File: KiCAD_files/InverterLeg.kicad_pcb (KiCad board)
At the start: 4 copper layers, 29 x 75 mm, 63 parts, among them J803 Conn_01x01_Pin, J806 Conn_01x01_Pin, J811 Screw_Terminal_01x01, J814 Screw_Terminal_01x01, J817 Screw_Terminal_01x01, J825 Conn_02x02_Top_Bottom, J827 Conn_02x02_Top_Bottom, J831 Conn_02x02_Top_Bottom, Q801 IPT60R055CM8, Q802 IPT60R055CM8, T801 CMB1670V, T802 CMB1670V, U603 UCC21222DR, U704 VPS8701B, U707 VPS8701B, U811 TMP117xxDRV, U815 TMP117xxDRV

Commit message: First routing complete.
Signed-off-by: Jean Alinei <jean.alinei@owntech.org>
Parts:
- removed R710: 4.7k, Resistor_SMD:R_0603_1608Metric
- added C718: 10uF, Capacitor_SMD:C_0805_2012Metric, F.Cu at (142.4, 91.2)
- added C719: 10uF, Capacitor_SMD:C_0805_2012Metric, F.Cu at (159.4, 90.7)
- added R610: 51R, Resistor_SMD:R_0402_1005Metric, F.Cu at (159.2, 96.5)
- added R611: 51R, Resistor_SMD:R_0402_1005Metric, F.Cu at (159.3, 97.4)
- added R612: 51R, Resistor_SMD:R_0402_1005Metric, F.Cu at (139.5, 96.1)
- added R613: 51R, Resistor_SMD:R_0402_1005Metric, F.Cu at (139.5, 95.2)
- added U801: LT1761-SD, Package_TO_SOT_SMD:TSOT-23-5, F.Cu at (158.6, 94.4)
- added U802: LT1761-SD, Package_TO_SOT_SMD:TSOT-23-5, F.Cu at (138.4, 93.2)
- U603: footprint Package_SO:SOIC-16W_7.5x10.3mm_P1.27mm -> Footprints:SOIC-16W_7.5x10.3mm_P1.27mm
- moved C734 3.10 mm to (155.8, 94.2), turned to -90 degrees
- moved C614 3.00 mm to (144.9, 89.5)
- moved C616 3.00 mm to (141.8, 89.1), turned to 0 degrees
- moved D710 2.66 mm to (156.4, 96.8)
- moved R605 2.60 mm to (154.7, 73.9)
- moved C602 2.60 mm to (152.3, 77.6)
- moved C604 2.60 mm to (152.3, 76.1)
- moved C605 2.60 mm to (147.0, 76.8)
- moved C607 2.60 mm to (149.3, 76.1)
- moved C703 2.60 mm to (155.4, 76.1)
- moved J831 2.60 mm to (148.6, 72.0)
- moved R606 2.60 mm to (153.1, 73.9)
- moved R609 2.60 mm to (149.3, 77.6)
- moved T801 2.60 mm to (150.0, 94.1)
- moved U603 2.60 mm to (151.2, 84.3)
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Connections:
- C717 pad 1: /12V_{LS} -> /12V_{LSRAW}
- C731 pad 1: /12V_{LS} -> /12V_{LSRAW}
- C734 pad 1: /12V_{HS} -> Net-(D709-K)
- D703 pad 1: /12V_{LS} -> /12V_{LSRAW}
- D704 pad 1: /12V_{LS} -> /12V_{LSRAW}
- D709 pad 1: /12V_{HS} -> Net-(D709-K)
- D710 pad 1: /12V_{HS} -> Net-(D709-K)
- L706 pad 1: /12V_{LS} -> /12V_{LSRAW}
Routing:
- net /GND_{LS}: track 0.00 -> 25.8 mm, vias 6 -> 11
- net /12V_{LS}: track 0.00 -> 16.5 mm, vias 1 -> 4
- net Net-(U704-VIN): track 0.00 -> 8.29 mm
- net /K_{SWN}: track 5.17 -> 13.0 mm, vias 3 -> 5
- net /12V_{PGND}: track 0.00 -> 7.55 mm
- net /12V_{HS}: track 2.80 -> 9.07 mm
- net Net-(U707-VIN): track 6.83 -> 12.3 mm
- net Net-(U704-VD1): track 0.00 -> 3.73 mm
- net Net-(U704-VD2): track 0.00 -> 3.37 mm
- net /5V_{DGND}: track 25.6 -> 22.4 mm
- net Net-(U707-VD1): track 0.00 -> 3.14 mm
- net Net-(U707-VD2): track 0.00 -> 2.86 mm
- net Net-(D709-K): track 0.00 -> 2.75 mm, vias 0 -> 2
- net /EN: track 0.00 -> 2.73 mm
- net /PWM_{LS}: track 20.1 -> 17.5 mm
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- added copper zone on F.Cu, net /12V_{HS}
- added copper zone on F.Cu, net /12V_{LSRAW}
- added copper zone on B.Cu, net /GND_{LS}
- added copper zone on B.Cu, net /SWN
- added copper zone on B.Cu, net /V_{IHigh_PGND}
- added copper zone on F.Cu, net Net-(D709-K)
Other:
- board size 29 x 75 mm -> 29 x 73 mm

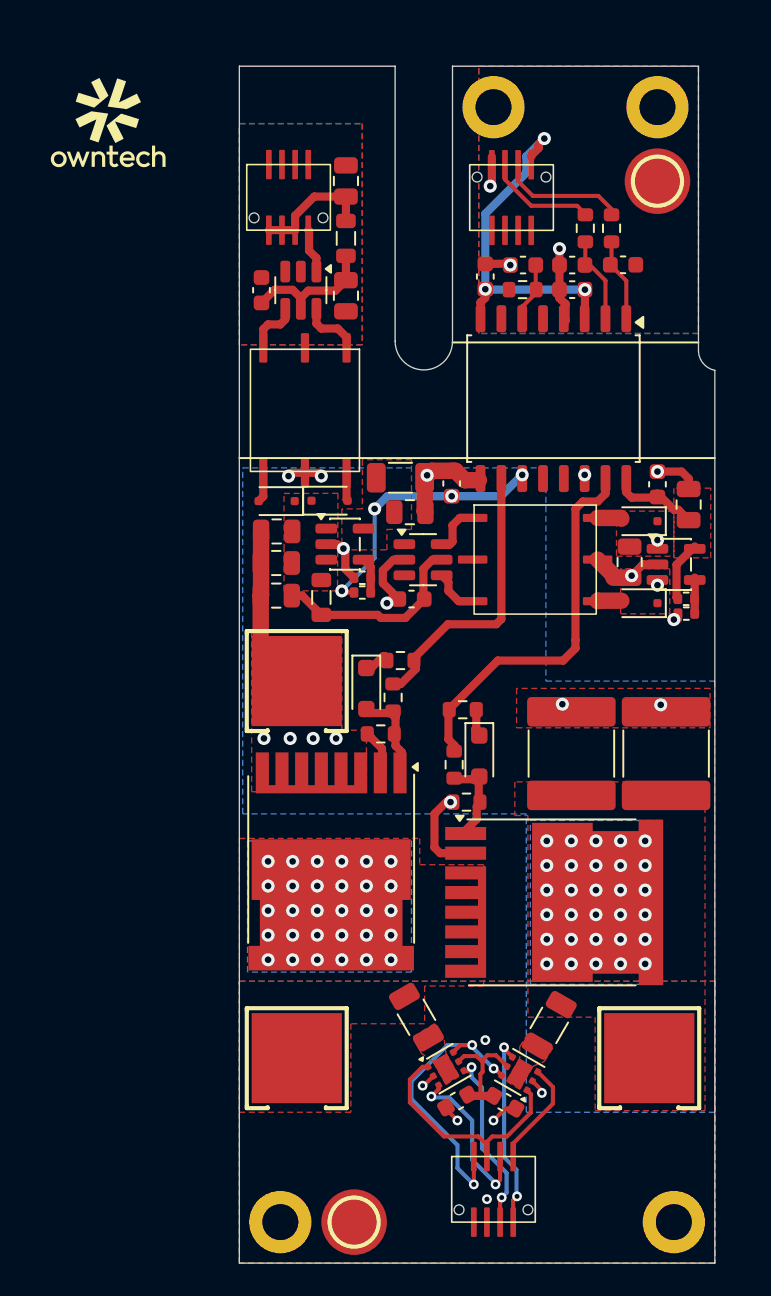
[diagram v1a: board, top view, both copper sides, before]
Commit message: Added gate coax. Added IPC2221 B1 rules. Changed diode footprints. Completed layout.
Signed-off-by: Jean Alinei <jean.alinei@owntech.org>
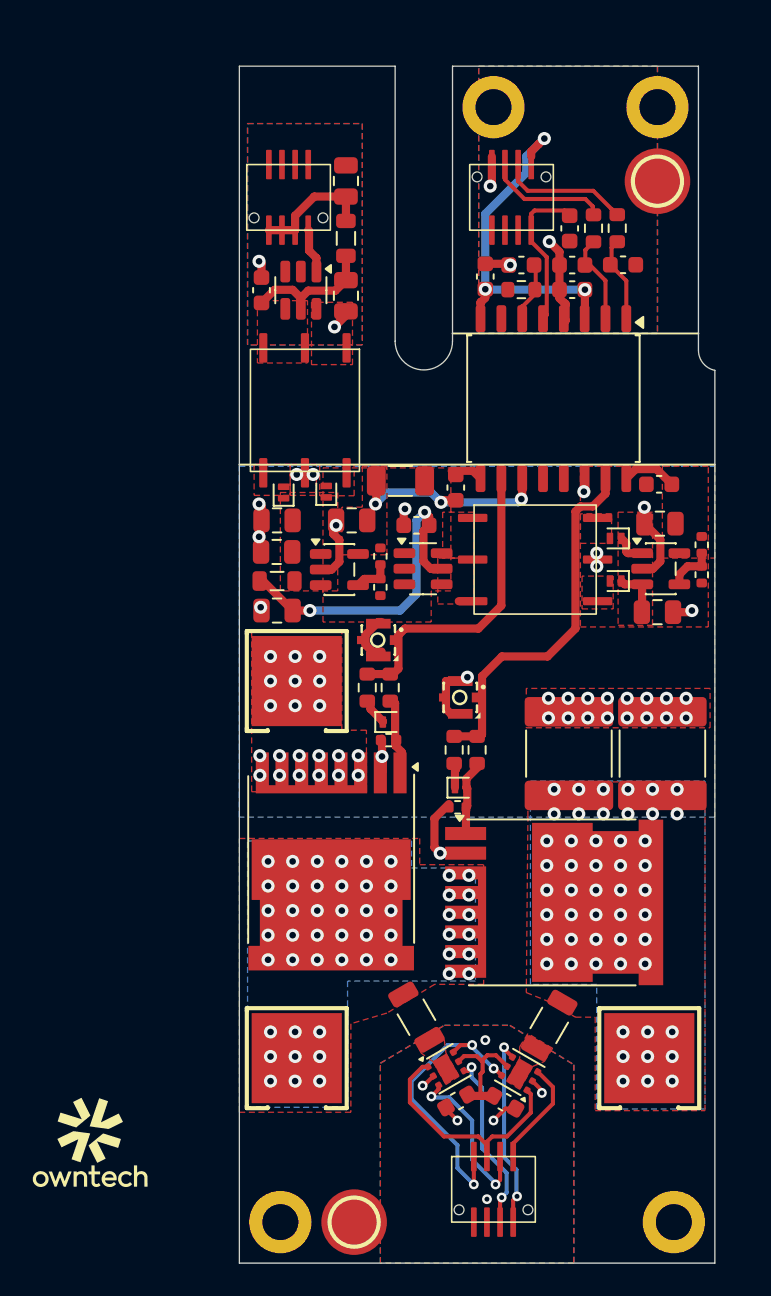
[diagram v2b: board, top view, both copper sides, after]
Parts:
- added C608: 100nF, Capacitor_SMD:C_0603_1608Metric, F.Cu at (152.1, 73.9)
- added J801: Conn_Coaxial_Small, Footprints:IPEX-SMD_4P-L1.7-W1.7-LS2.0-L-4, F.Cu at (145.5, 102.5)
- added J802: Conn_Coaxial_Small, Footprints:IPEX-SMD_4P-L1.7-W1.7-LS2.0-L-4, F.Cu at (140.5, 99.0)
- D601: footprint Diode_SMD:D_SOD-323_HandSoldering -> Diode_SMD:D_SOD-882
- D602: value PMEG3010CEJ,115 -> ~; footprint Diode_SMD:D_SOD-323_HandSoldering -> Diode_SMD:D_SOD-882
- D703, D704, D709, D710: footprint Diode_SMD:D_SOD-323F -> Diode_SMD:D_SOD-882
- R607, R608: footprint Resistor_SMD:R_0603_1608Metric -> Resistor_SMD:R_0402_1005Metric
- TJ801, TJ804: footprint Resistor_SMD:R_1206_3216Metric -> Footprints:THJP_1206_3216Metric
- moved G*** 62.2 mm to (122.9, 128.9)
- moved G*** 62.2 mm to (122.9, 131.7)
- moved C733 4.51 mm to (142.8, 92.0)
- moved C718 3.59 mm to (138.8, 91.7), turned to 180 degrees
- moved C734 3.49 mm to (157.5, 97.3), turned to 0 degrees
- moved R610 3.43 mm to (160.2, 93.2), turned to 90 degrees
- moved L706 2.88 mm to (134.3, 95.4), turned to 180 degrees
- moved R603 2.61 mm to (139.8, 101.9), turned to -90 degrees
- moved R611 2.55 mm to (160.2, 95.0), turned to 90 degrees
- moved R601 2.51 mm to (145.1, 105.7), turned to -90 degrees
- moved R612 2.47 mm to (140.6, 93.9), turned to 90 degrees
- moved D601 2.45 mm to (141.1, 104.0), turned to 0 degrees
- moved D602 2.24 mm to (145.5, 108.0), turned to 0 degrees
- moved C719 2.10 mm to (157.7, 91.9), turned to 180 degrees
- moved D710 1.98 mm to (154.9, 95.4)
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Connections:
- C614 pad 2: /GND_{LS} -> /K_{GNDLS}
- C616 pad 2: /GND_{LS} -> /K_{GNDLS}
- C717 pad 2: /GND_{LS} -> /K_{GNDLS}
- C718 pad 2: /GND_{LS} -> /K_{GNDLS}
- C731 pad 2: /GND_{LS} -> /K_{GNDLS}
- C732 pad 2: /GND_{LS} -> /K_{GNDLS}
- C733 pad 2: /GND_{LS} -> /K_{GNDLS}
- J831 pad 8: unconnected-(J831-Pin_8-Pad8) -> /DIS
- Q801 pad 2: Net-(Q801-DS) -> /K_{GNDLS}
- R608 pad 1: Net-(Q801-DS) -> /K_{GNDLS}
- R613 pad 1: /GND_{LS} -> /K_{GNDLS}
- T802 pad 5: /GND_{LS} -> /K_{GNDLS}
- U603 pad 9: /GND_{LS} -> /K_{GNDLS}
- U707 pad 2: /GND_{LS} -> /K_{GNDLS}
- U802 pad 2: /GND_{LS} -> /K_{GNDLS}
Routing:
- net /GND_{LS}: track 25.8 -> 0.00 mm, vias 11 -> 37
- net /K_{GNDLS}: track 0.00 -> 17.7 mm, vias 0 -> 8
- net /DIS: track 0.00 -> 9.45 mm
- net Net-(U707-VIN): track 12.3 -> 20.5 mm, vias 0 -> 2
- net /12V_{HS}: track 9.07 -> 3.40 mm
- net Net-(U704-VD1): track 3.73 -> 0.00 mm
- net /K_{SWN}: track 13.0 -> 16.5 mm, vias 5 -> 7
- net Net-(U704-VD2): track 3.37 -> 0.00 mm
- net /12V_{LS}: track 16.5 -> 13.2 mm, vias 4 -> 3
- net Net-(U707-VD1): track 3.14 -> 0.00 mm
- net Net-(Q801-DS): track 2.62 -> 0.00 mm
- net /PGND: track 4.60 -> 6.89 mm, vias 6 -> 8
- net Net-(U707-VD2): track 2.86 -> 0.85 mm
- net Net-(D704-A): track 1.84 -> 0.00 mm
- net Net-(D703-A): track 1.72 -> 0.00 mm
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- added copper zone on F.Cu, net /K_{GNDLS}
- added copper zone on In1.Cu, net /K_{GNDLS}
- added copper zone on F.Cu, net /K_{SWN}
- added copper zone on F.Cu, net Net-(D703-A)
- added copper zone on F.Cu, net Net-(D704-A)
- added copper zone on F.Cu, net Net-(D709-A)
- added copper zone on F.Cu, net Net-(D710-A)
- added copper zone on F.Cu, net Net-(U704-VD1)
- added copper zone on F.Cu, net Net-(U704-VD2)
- added copper zone on F.Cu, net Net-(U707-VD1)
- added copper zone on F.Cu, net Net-(U707-VD2)

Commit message: Added SMTSO footprints to replace cube screw terminals. Added header for optional fan
Signed-off-by: Jean Alinei <jean.alinei@owntech.org>
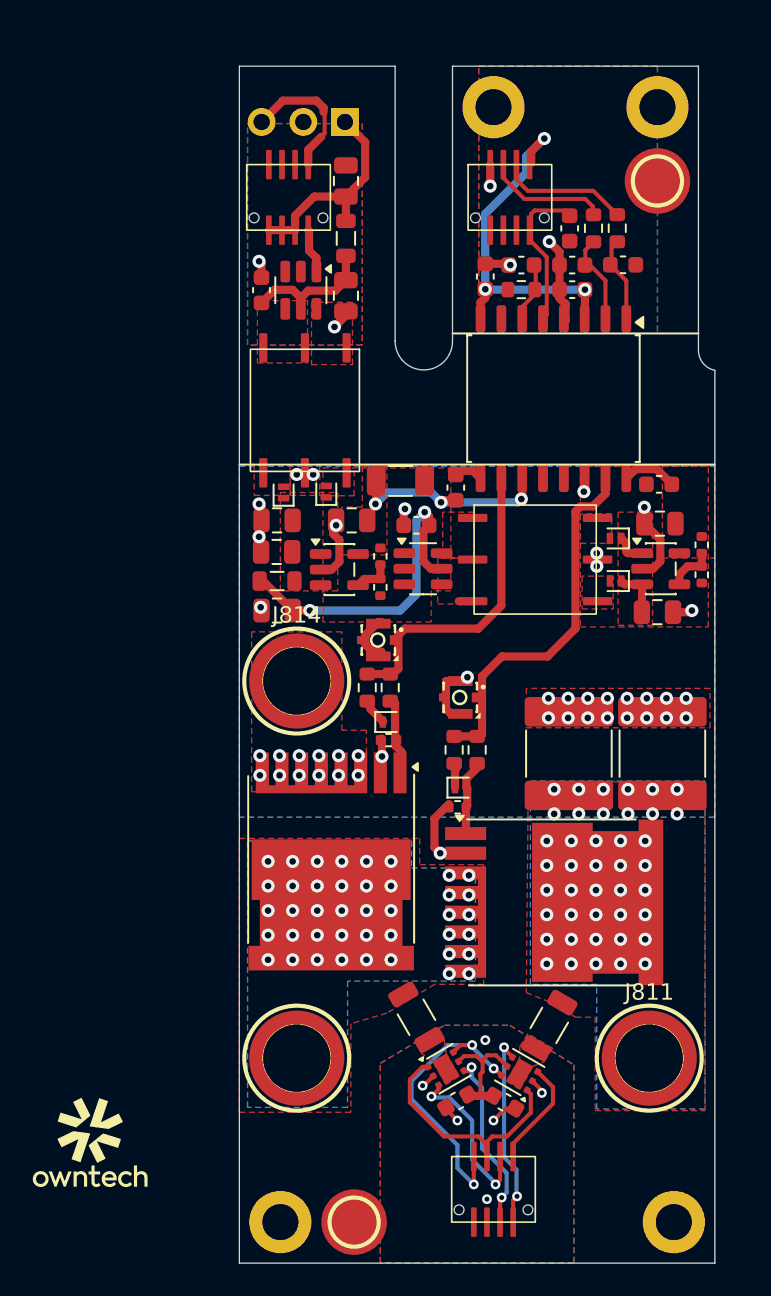
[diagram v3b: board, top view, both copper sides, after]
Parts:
- added J804: Conn_01x03_Socket, Connector_PinHeader_2.54mm:PinHeader_1x03_P2.54mm_Vertical, B.Cu at (138.4, 67.4)
- J811, J814, J817: footprint Footprints:SMD_L5.0-W5.0_CON1_5X5_SMD -> Footprints:SMD-1_BD5.5-D4.0_H5
- moved J831 0.10 mm to (148.5, 72.0), turned to 0 degrees
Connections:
- J825 pad 5: /PGND -> /SPEED
- J831 pad 1: /5V_{DGND} -> unconnected-(J831-Pin_1-Pad1)
- J831 pad 2: /PWMH_{MCU} -> unconnected-(J831-Pin_2-Pad2)
- J831 pad 3: /PWML_{MCU} -> unconnected-(J831-Pin_3-Pad3)
- J831 pad 4: DGND -> /DIS
- J831 pad 5: unconnected-(J831-Pin_5-Pad5) -> /5V_{DGND}
- J831 pad 6: unconnected-(J831-Pin_6-Pad6) -> /PWMH_{MCU}
- J831 pad 7: unconnected-(J831-Pin_7-Pad7) -> /PWML_{MCU}
- J831 pad 8: /DIS -> DGND
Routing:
- net /SPEED: track 0.00 -> 8.40 mm
- net /12V_{PGND}: track 7.55 -> 13.1 mm
- net Net-(U603-DT): track 4.01 -> 3.01 mm
- net DGND: track 8.84 -> 8.31 mm
- net /V_{IHigh_PGND}: vias 51 -> 42
- net /SWN: vias 51 -> 42
- net /GND_{LS}: vias 37 -> 28

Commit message: Tidied up schematic - Final height for SMTSO 5mm
Signed-off-by: Jean Alinei <jean.alinei@owntech.org>
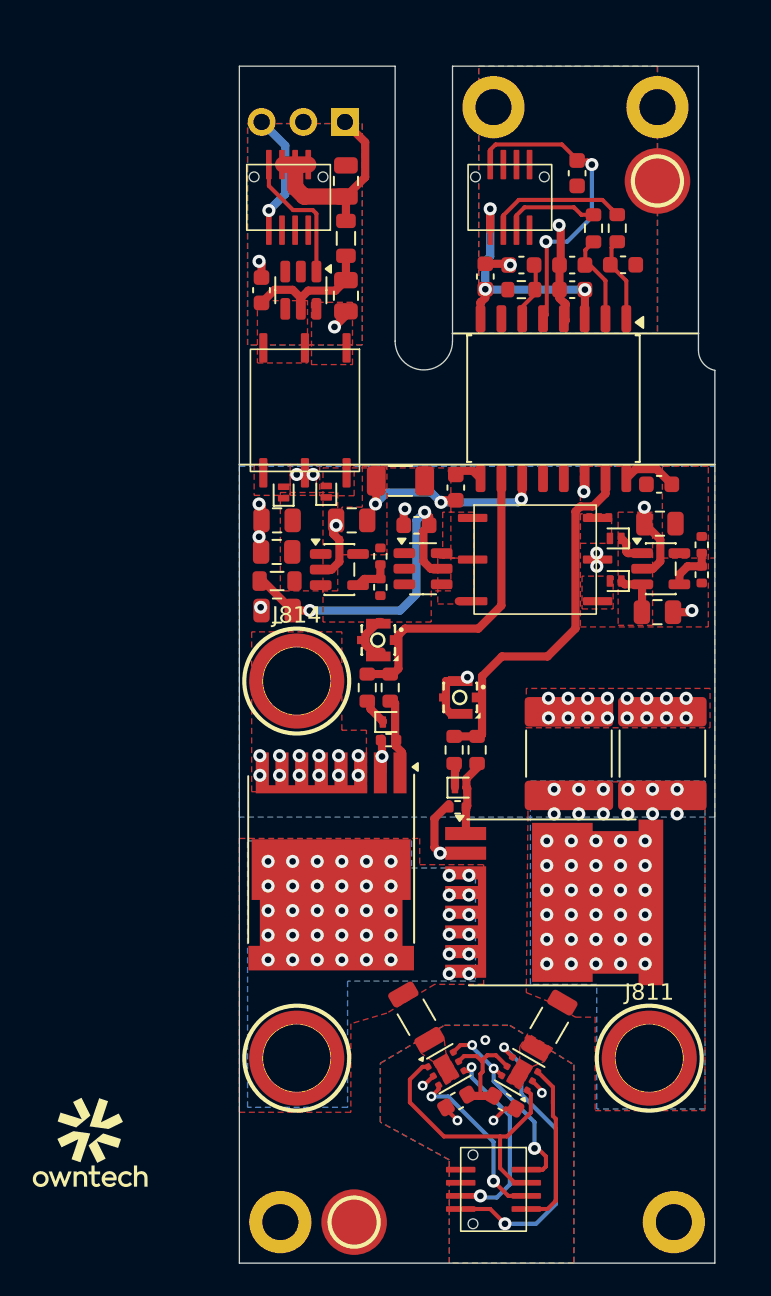
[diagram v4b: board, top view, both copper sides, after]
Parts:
- moved C608 3.40 mm to (152.6, 70.5)
- turned J825 to 180 degrees
- turned J827 to -90 degrees
- turned J831 to 180 degrees
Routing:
- net /DIS: track 9.45 -> 19.2 mm, vias 0 -> 2
- net /ADDR_HS: track 11.9 -> 18.4 mm
- net /5V_{DGND}: track 22.8 -> 16.6 mm
- net /EN: track 2.73 -> 8.43 mm
- net /SDA_{PWR}: track 18.2 -> 12.7 mm
- net /ALERT_HS: track 6.56 -> 10.5 mm
- net /SCL_{PWR}: track 15.1 -> 17.0 mm
- net /PWML_{MCU}: track 7.52 -> 5.99 mm
- net /SPEED: track 8.40 -> 7.61 mm, vias 0 -> 1
- net DGND: track 8.31 -> 7.81 mm, vias 3 -> 2
- net /PGND: vias 8 -> 7

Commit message: the schematic has no more ERC and the DRC are on their way
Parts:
- added REF**: Symbol_Hot_Surface_Triangle_6x6mm_Silkscreen, Footprints:Symbol_HighVoltage_Triangle_6x6mm_Copper, B.Cu at (146.1, 106.6)
- added kibuzzard-6A8EFBEE: G***, kibuzzard-6A8EFBEE, B.Cu at (135.9, 64.9)
- added kibuzzard-6A8EFC0A: G***, kibuzzard-6A8EFC0A, B.Cu at (138.4, 64.9)
- added kibuzzard-6A8EFC24: G***, kibuzzard-6A8EFC24, B.Cu at (133.4, 64.9)
- added kibuzzard-6A8EFC43: G***, kibuzzard-6A8EFC43, B.Cu at (135.9, 70.2)
- J825, J827, J831: value Conn_02x02_Top_Bottom -> HC-PBB08-2-08-M-H4.0-G1-R-P-04
- R610, R612: value 51R -> 176.8k
- R611, R613: value 51R -> 20k
- U603: value UCC21222DR -> ~
- moved G*** 6.10 mm to (126.4, 123.9)
- moved G*** 6.10 mm to (126.4, 126.7)
- moved R605 0.25 mm to (154.8, 73.9)
- moved R606 0.25 mm to (153.4, 73.9)
- moved L703 0.13 mm to (138.6, 74.5)
- moved C713 0.07 mm to (133.3, 77.7)
- moved C709 0.06 mm to (138.6, 71.0)
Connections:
- net /12V_{PGND} renamed +12V_PGND
- net /5V_{DGND} renamed +5V_DGND
- C709 pad 2: /PGND -> PGND2
- C711 pad 2: /PGND -> PGND2
- C713 pad 2: /PGND -> PGND2
- C751 pad 1: /5V_{PGND} -> +5V_PGND
- C751 pad 2: /PGND -> PGND
- C754 pad 1: /5V_{PGND} -> +5V_PGND
- C754 pad 2: /PGND -> PGND
- H801 pad 1: Earth_Protective -> Earth_Protective1
- H802 pad 1: Earth_Protective -> Earth_Protective2
- H803 pad 1: Earth_Protective -> Earth_Protective3
- H804 pad 1: Earth_Protective -> Earth_Protective4
- J803 pad 1: Earth_Protective -> Earth_Protective3
- J804 pad 2: /PGND -> PGND2
- J806 pad 1: Earth_Protective -> Earth_Protective2
- J825 pad 4: /EN -> /SPEED
- J825 pad 5: /SPEED -> PGND2
- J825 pad 6: /PGND -> PGND2
- J825 pad 7: /PGND -> PGND2
- J825 pad 8: /PGND -> /EN
- J827 pad 1: /5V_{LS} -> +5V_PGND
- J827 pad 2: /PGND -> PGND
- U704 pad 2: /PGND -> PGND2
- U811 pad 2: /PGND -> PGND
- U811 pad 5: /5V_{PGND} -> +5V_PGND
- U815 pad 2: /PGND -> PGND
- U815 pad 5: /5V_{PGND} -> +5V_PGND
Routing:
- net +12V_PGND: track 13.3 -> 1.81 mm
- net /5V_{PGND}: track 7.36 -> 0.00 mm
- net +5V_PGND: track 0.00 -> 7.36 mm
- net /PGND: track 6.89 -> 0.00 mm, vias 7 -> 0
- net /EN: track 8.43 -> 2.75 mm
- net /SPEED: track 7.61 -> 2.78 mm, vias 1 -> 0
- net PGND: track 0.00 -> 4.60 mm, vias 0 -> 5
- net PGND2: track 0.00 -> 2.26 mm, vias 0 -> 8
- added copper zone on F.Cu, net +12V_PGND
- added copper zone on F.Cu, net Earth_Protective2
- added copper zone on F.Cu, net Earth_Protective3
- added copper zone on B.Cu, net PGND
- added copper zone on F.Cu, net PGND
- added copper zone on In1.Cu, net PGND
- added copper zone on In2.Cu, net PGND
- added copper zone on B.Cu, net PGND2
- added copper zone on F.Cu, net PGND2
- added copper zone on In1.Cu, net PGND2
- added copper zone on In2.Cu, net PGND2
- removed copper zone on B.Cu, net /PGND
- removed copper zone on F.Cu, net /PGND
- removed copper zone on In1.Cu, net /PGND
- removed copper zone on In2.Cu, net /PGND
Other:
- board text added: "M2"

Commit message: schematic tidy-up and traces wip
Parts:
- removed REF**: Symbol_Hot_Surface_Triangle_6x6mm_Silkscreen, Footprints:Symbol_HighVoltage_Triangle_6x6mm_Copper
- added TP801: ~, TestPoint:TestPoint_Pad_D1.0mm, F.Cu at (154.4, 70.4)
- added TP802: ~, TestPoint:TestPoint_Pad_D1.0mm, F.Cu at (152.6, 71.4)
- added TP803: ~, TestPoint:TestPoint_Pad_D1.0mm, F.Cu at (154.4, 68.4)
- added TP804: ~, TestPoint:TestPoint_Pad_D1.0mm, F.Cu at (152.6, 69.4)
- added TP805: ~, TestPoint:TestPoint_Pad_D1.0mm, F.Cu at (136.8, 75.4)
- added TP806: ~, TestPoint:TestPoint_Pad_D1.0mm, F.Cu at (133.2, 76.0)
- added TP807: ~, TestPoint:TestPoint_Pad_D1.0mm, F.Cu at (138.4, 65.4)
- added TP808: ~, TestPoint:TestPoint_Pad_D1.0mm, F.Cu at (135.9, 65.4)
- added TP809: ~, TestPoint:TestPoint_Pad_D1.0mm, F.Cu at (133.4, 65.4)
- added TP810: ~, TestPoint:TestPoint_Pad_D1.0mm, F.Cu at (160.1, 90.1)
- added TP811: ~, TestPoint:TestPoint_Pad_D1.0mm, F.Cu at (160.1, 97.1)
- added TP812: ~, TestPoint:TestPoint_Pad_D1.0mm, F.Cu at (140.5, 91.8)
- added TP813: ~, TestPoint:TestPoint_Pad_D1.0mm, F.Cu at (143.1, 97.3)
- added TP814: ~, TestPoint:TestPoint_Pad_D1.0mm, F.Cu at (137.9, 97.3)
- added TP815: ~, TestPoint:TestPoint_Pad_D1.0mm, F.Cu at (151.1, 128.8)
- added TP816: ~, TestPoint:TestPoint_Pad_D1.0mm, F.Cu at (151.1, 130.8)
- added TP817: ~, TestPoint:TestPoint_Pad_D1.0mm, F.Cu at (151.1, 132.8)
- added TP818: ~, TestPoint:TestPoint_Pad_D1.0mm, F.Cu at (151.1, 134.9)
- added TP819: ~, TestPoint:TestPoint_Pad_D1.0mm, F.Cu at (143.0, 128.6)
- added TP820: ~, TestPoint:TestPoint_Pad_D1.0mm, F.Cu at (146.6, 128.6)
- added TP821: ~, TestPoint:TestPoint_Pad_D1.0mm, F.Cu at (147.5, 136.1)
- added TP822: ~, TestPoint:TestPoint_Pad_D1.0mm, F.Cu at (149.5, 136.1)
- moved C608 2.98 mm to (151.9, 67.6), turned to 180 degrees
- moved C718 0.97 mm to (137.9, 91.8)
- moved C713 0.82 mm to (133.3, 78.5)
- moved U704 0.41 mm to (135.8, 78.1)
- moved C703 0.37 mm to (155.8, 76.1)
- moved C604 0.37 mm to (152.7, 76.1)
- moved C751 0.36 mm to (148.3, 127.5)
- moved C734 0.26 mm to (157.2, 97.3)
- moved C754 0.22 mm to (145.2, 127.3)
- moved C614 0.21 mm to (145.0, 89.7)
- moved U815 0.17 mm to (149.1, 125.6)
- moved U802 0.15 mm to (138.1, 94.5)
- moved D709 0.10 mm to (154.8, 92.8)
- moved D710 0.10 mm to (154.8, 95.4)
- moved R605 0.08 mm to (154.9, 73.9)
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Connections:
- net Net-(D709-K) renamed /12V_{HSRAW}
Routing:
- net PGND: track 4.60 -> 21.6 mm, vias 5 -> 11
- net +5V_PGND: track 7.36 -> 18.9 mm
- net /ALERT_LS: track 10.6 -> 19.7 mm
- net /ADDR_LS: track 10.8 -> 17.2 mm, vias 2 -> 3
- net /PWM_{HS}: track 22.7 -> 17.2 mm
- net /K_{GNDLS}: track 17.7 -> 12.2 mm, vias 8 -> 12
- net /ADDR_HS: track 18.4 -> 21.8 mm
- net /SCL_{PWR}: track 17.0 -> 13.6 mm, vias 0 -> 2
- net /PWMH_{MCU}: track 8.41 -> 11.2 mm
- net PGND2: track 2.26 -> 4.86 mm
- net /ALERT_HS: track 10.5 -> 12.9 mm
- net /SDA_{PWR}: track 12.7 -> 15.0 mm, vias 3 -> 4
- net /12V_{LSRAW}: track 0.00 -> 2.19 mm
- net /DIS: track 19.5 -> 21.6 mm
- net Net-(U707-VIN): track 20.5 -> 22.6 mm
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- added copper zone on B.Cu, net /K_{SWN}
- added copper zone on In2.Cu, net /K_{SWN}
